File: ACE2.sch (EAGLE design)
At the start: 141 parts, among them IC1 7805T, Q1 2N3904, Q2 2N3904, Q3 BC237, X1 6M5

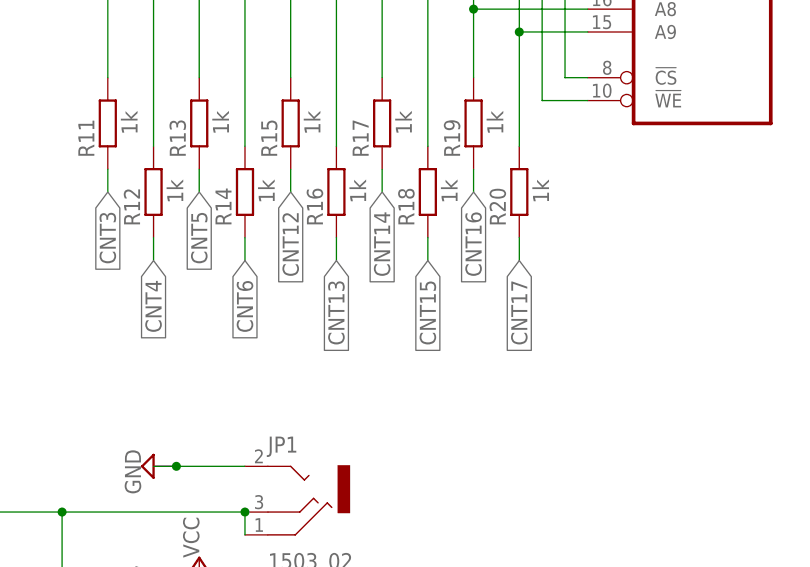
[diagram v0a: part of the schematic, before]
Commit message: Correct problem the CNT8 as input for Video Screen Access.
Signed-off-by: John Bradley <flypie@rocketmail.com>
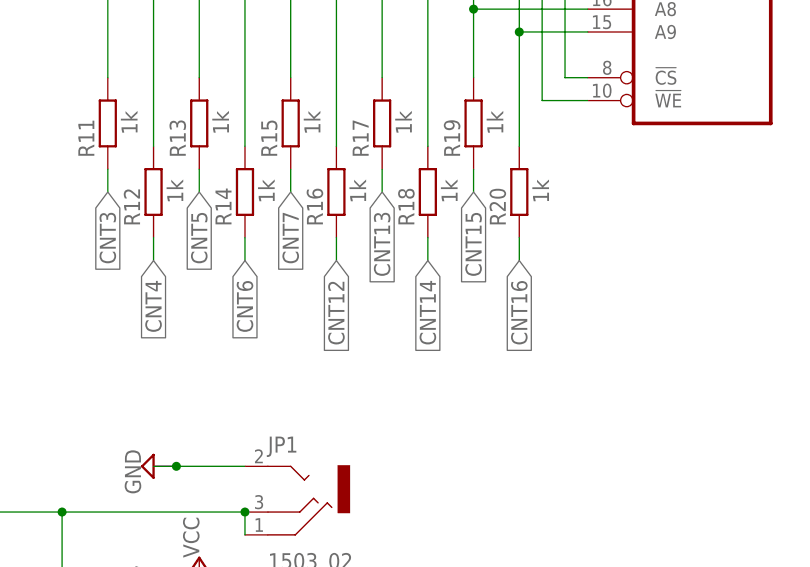
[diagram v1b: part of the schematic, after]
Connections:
- net CNT12: now also R16.1; no longer R15.1
- net CNT13: now also R17.1; no longer R16.1
- net CNT14: now also R18.1; no longer R17.1
- net CNT15: now also R19.1; no longer R18.1
- net CNT16: now also R20.1; no longer R19.1
- net CNT17: no longer R20.1
- net CNT7: now also R15.1
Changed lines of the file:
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@@
-</segment>
-<segment>
-<pinref part="R19" gate="G$1" pin="1"/>
-<wire x1="149.86" y1="-147.32" x2="149.86" y2="-149.86" width="0.1524" layer="91"/>
-<label x="149.86" y="-149.86" size="1.778" layer="95" rot="R270" xref="yes"/>
 </segment>
 <segment>
@@
 <label x="304.8" y="-320.04" size="1.778" layer="95" rot="R90" xref="yes"/>
 </segment>
+<segment>
+<pinref part="R20" gate="G$1" pin="1"/>
+<wire x1="154.94" y1="-154.94" x2="154.94" y2="-157.48" width="0.1524" layer="91"/>
+<label x="154.94" y="-157.48" size="1.778" layer="95" rot="R270" xref="yes"/>
+</segment>
 </net>
 <net name="CNT15" class="0">
@@
 <wire x1="355.6" y1="-284.48" x2="353.06" y2="-284.48" width="0.1524" layer="91"/>
 <label x="353.06" y="-284.48" size="1.778" layer="95" rot="R180" xref="yes"/>
-</segment>
-<segment>
-<pinref part="R18" gate="G$1" pin="1"/>
-<wire x1="144.78" y1="-154.94" x2="144.78" y2="-157.48" width="0.1524" layer="91"/>
-<label x="144.78" y="-157.48" size="1.778" layer="95" rot="R270" xref="yes"/>
 </segment>
 <segment>
@@
 <wire x1="271.78" y1="-320.04" x2="274.32" y2="-320.04" width="0.1524" layer="91"/>
 </segment>
+<segment>
+<pinref part="R19" gate="G$1" pin="1"/>
+<wire x1="149.86" y1="-147.32" x2="149.86" y2="-149.86" width="0.1524" layer="91"/>
+<label x="149.86" y="-149.86" size="1.778" layer="95" rot="R270" xref="yes"/>
+</segment>
 </net>
 <net name="CNT17" class="0">
@@
 <label x="81.28" y="55.88" size="1.778" layer="95" rot="R180" xref="yes"/>
 <pinref part="Z25" gate="A" pin="I0"/>
-</segment>
-<segment>
-<pinref part="R20" gate="G$1" pin="1"/>
-<wire x1="154.94" y1="-154.94" x2="154.94" y2="-157.48" width="0.1524" layer="91"/>
-<label x="154.94" y="-157.48" size="1.778" layer="95" rot="R270" xref="yes"/>
 </segment>
 <segment>
@@
 <wire x1="299.72" y1="-254" x2="317.5" y2="-254" width="0.1524" layer="91"/>
 </segment>
+<segment>
+<pinref part="R15" gate="G$1" pin="1"/>
+<wire x1="129.54" y1="-147.32" x2="129.54" y2="-149.86" width="0.1524" layer="91"/>
+<label x="129.54" y="-149.86" size="1.778" layer="95" rot="R270" xref="yes"/>
+</segment>
 </net>
 <net name="CNT6" class="0">
@@
 <net name="CNT14" class="0">
 <segment>
-<pinref part="R17" gate="G$1" pin="1"/>
-<wire x1="139.7" y1="-147.32" x2="139.7" y2="-149.86" width="0.1524" layer="91"/>
-<label x="139.7" y="-149.86" size="1.778" layer="95" rot="R270" xref="yes"/>
-</segment>
-<segment>
 <pinref part="Z11" gate="A" pin="QC"/>
 <label x="314.96" y="-302.26" size="1.778" layer="95" rot="R90" xref="yes"/>
@@
 <wire x1="299.72" y1="-302.26" x2="320.04" y2="-302.26" width="0.1524" layer="91"/>
 </segment>
+<segment>
+<pinref part="R18" gate="G$1" pin="1"/>
+<wire x1="144.78" y1="-154.94" x2="144.78" y2="-157.48" width="0.1524" layer="91"/>
+<label x="144.78" y="-157.48" size="1.778" layer="95" rot="R270" xref="yes"/>
+</segment>
 </net>
 <net name="CNT12" class="0">
-<segment>
-<pinref part="R15" gate="G$1" pin="1"/>
-<wire x1="129.54" y1="-147.32" x2="129.54" y2="-149.86" width="0.1524" layer="91"/>
-<label x="129.54" y="-149.86" size="1.778" layer="95" rot="R270" xref="yes"/>
-</segment>
 <segment>
 <pinref part="Z11" gate="A" pin="QA"/>
@@
 <wire x1="299.72" y1="-297.18" x2="320.04" y2="-297.18" width="0.1524" layer="91"/>
 </segment>
-</net>
-<net name="CNT13" class="0">
 <segment>
 <pinref part="R16" gate="G$1" pin="1"/>
@@
 <label x="134.62" y="-157.48" size="1.778" layer="95" rot="R270" xref="yes"/>
 </segment>
+</net>
+<net name="CNT13" class="0">
 <segment>
 <pinref part="Z11" gate="A" pin="QB"/>
@@
 <wire x1="299.72" y1="-299.72" x2="320.04" y2="-299.72" width="0.1524" layer="91"/>
 </segment>
-</net>
+<segment>
+<pinref part="R17" gate="G$1" pin="1"/>
+<wire x1="139.7" y1="-147.32" x2="139.7" y2="-149.86" width="0.1524" layer="91"/>
+<label x="139.7" y="-149.86" size="1.778" layer="95" rot="R270" xref="yes"/>
+</segment>
+</net>

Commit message: Minor changes update  crystal.
Signed-off-by: John Bradley <flypie@rocketmail.com>
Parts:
- X1: value 6M5 -> 6.556MHz; device crystal:HC49GW -> crystal:CRYSTALHC49U-V
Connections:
- net N$36: now also X1.1; no longer X1.2
- net N$47: now also X1.2; no longer X1.1
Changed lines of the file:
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@@
 <?xml version="1.0" encoding="utf-8"?>
 <!DOCTYPE eagle SYSTEM "eagle.dtd">
-<eagle version="9.3.2">
+<eagle version="9.4.0">
 <drawing>
 <settings>
@@
 <part name="R1" library="rcl" library_urn="urn:adsk.eagle:library:334" deviceset="R-EU_" device="0207/2V" package3d_urn="urn:adsk.eagle:package:23490/1" value="47k"/>
 <part name="Q1" library="transistor" library_urn="urn:adsk.eagle:library:402" deviceset="2N3904" device="" package3d_urn="urn:adsk.eagle:package:28523/2"/>
-<part name="X1" library="crystal" library_urn="urn:adsk.eagle:library:204" deviceset="HC49GW" device="" package3d_urn="urn:adsk.eagle:package:12072/1" value="6M5"/>
 <part name="R9" library="rcl" library_urn="urn:adsk.eagle:library:334" deviceset="R-EU_" device="0207/2V" package3d_urn="urn:adsk.eagle:package:23490/1" value="47k"/>
 <part name="P+16" library="supply1" library_urn="urn:adsk.eagle:library:371" deviceset="VCC" device=""/>
@@
 <part name="SUPPLY25" library="supply2" library_urn="urn:adsk.eagle:library:372" deviceset="GND" device=""/>
 <part name="P+23" library="supply1" library_urn="urn:adsk.eagle:library:371" deviceset="VCC" device=""/>
+<part name="X1" library="crystal" library_urn="urn:adsk.eagle:library:204" deviceset="CRYSTAL" device="HC49U-V" package3d_urn="urn:adsk.eagle:package:12075/1" value="6.556MHz"/>
 </parts>
 <sheets>
@@
 <attribute name="VALUE" x="220.98" y="-271.78" size="1.778" layer="96"/>
 </instance>
-<instance part="X1" gate="G$1" x="218.44" y="-256.54" smashed="yes">
-<attribute name="NAME" x="220.98" y="-255.524" size="1.778" layer="95"/>
-<attribute name="VALUE" x="220.98" y="-259.08" size="1.778" layer="96"/>
-</instance>
 <instance part="R9" gate="G$1" x="233.68" y="-251.46" smashed="yes" rot="R270">
 <attribute name="NAME" x="235.1786" y="-247.65" size="1.778" layer="95" rot="R270"/>
@@
 <attribute name="VALUE" x="-248.92" y="-335.28" size="1.778" layer="96" rot="R180"/>
 </instance>
+<instance part="X1" gate="G$1" x="218.44" y="-256.54" smashed="yes" rot="R180">
+<attribute name="NAME" x="215.9" y="-257.556" size="1.778" layer="95" rot="R180"/>
+<attribute name="VALUE" x="215.9" y="-254" size="1.778" layer="96" rot="R180"/>
+</instance>
 </instances>
 <busses>
@@
 <pinref part="C5" gate="G$1" pin="1"/>
 <wire x1="220.98" y1="-256.54" x2="223.52" y2="-256.54" width="0.1524" layer="91"/>
-<pinref part="X1" gate="G$1" pin="2"/>
+<pinref part="X1" gate="G$1" pin="1"/>
 </segment>
 </net>
@@
 <wire x1="213.36" y1="-271.78" x2="213.36" y2="-269.24" width="0.1524" layer="91"/>
 <wire x1="213.36" y1="-256.54" x2="213.36" y2="-264.16" width="0.1524" layer="91"/>
-<pinref part="X1" gate="G$1" pin="1"/>
 <wire x1="213.36" y1="-264.16" x2="213.36" y2="-269.24" width="0.1524" layer="91"/>
 <wire x1="213.36" y1="-256.54" x2="215.9" y2="-256.54" width="0.1524" layer="91"/>
 <junction x="213.36" y="-264.16"/>
 <junction x="213.36" y="-269.24"/>
+<pinref part="X1" gate="G$1" pin="2"/>
 </segment>
 </net>

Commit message: Correct component details and bus problem.
Signed-off-by: John Bradley <flypie@rocketmail.com>
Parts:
- Z14: value 74LS367D -> 74367N; device 74xx-eu:74LS367D -> 74xx-eu:74367N
- renumbered Z28 to Z12, Z29 to Z13
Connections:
- new net N$9: Z14A.1G
- net N$29: no longer Z14A.1G
